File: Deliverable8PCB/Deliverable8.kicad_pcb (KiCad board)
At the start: 2 copper layers, 55 parts, among them J2 PiHeaderM, Q1 NMOS, Q2 PMOS, U1 MCP4131-xxxx-P, U10 MCP4131-xxxx-P, U11 MCP4131-xxxx-P, U12 LM741, U2 LM741, U3 LM741, U4 LM339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

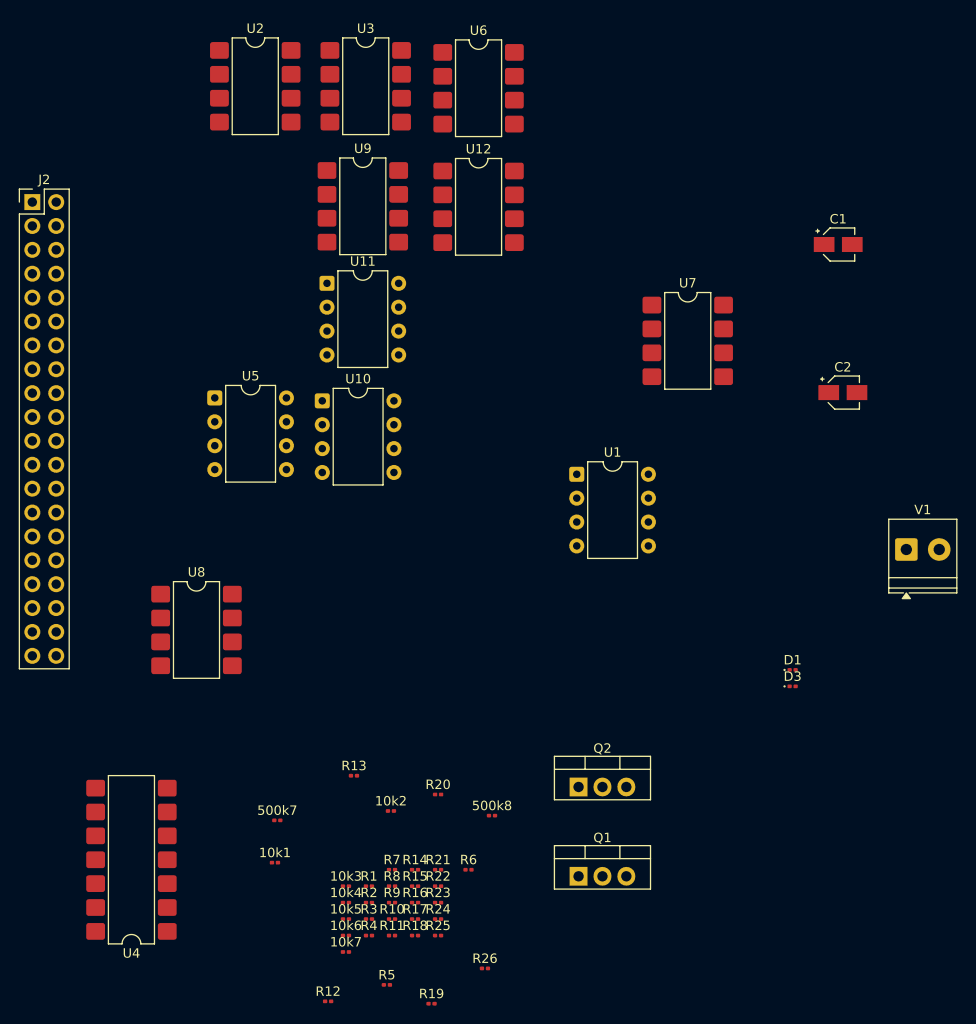
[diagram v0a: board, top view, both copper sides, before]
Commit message: update i2c_lcd
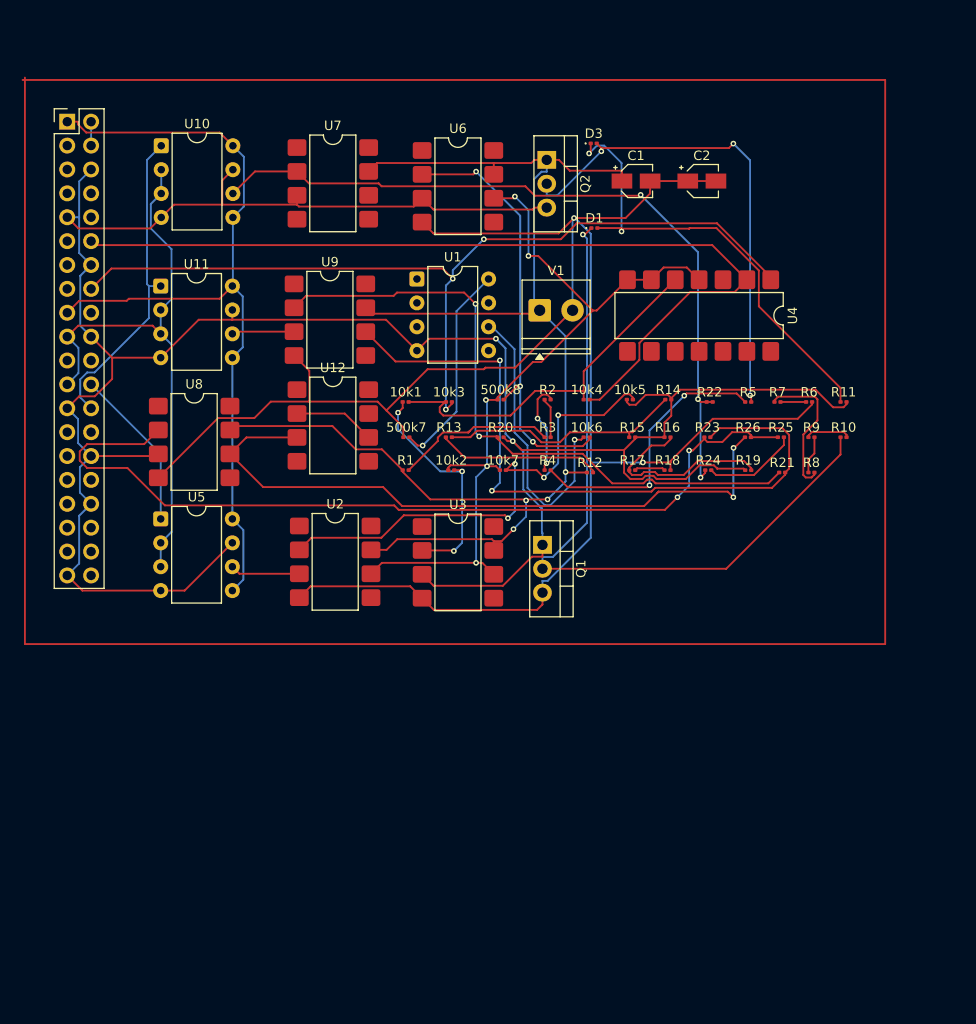
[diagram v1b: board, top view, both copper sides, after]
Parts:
- moved U4 83.6 mm to (109.7, 50.8), turned to -90 degrees
- moved R11 74.3 mm to (125.1, 60.0)
- moved R5 72.9 mm to (114.9, 60.0)
- moved R10 70.2 mm to (125.1, 63.8)
- moved Q2 66.8 mm to (93.5, 34.2), turned to -90 degrees
- moved R9 66.6 mm to (121.7, 63.8)
- moved R19 66.0 mm to (114.9, 67.2)
- moved R7 64.5 mm to (118.0, 60.0)
- moved R25 64.3 mm to (118.4, 63.8)
- moved R26 63.0 mm to (114.9, 63.8)
- moved 10k5 63.0 mm to (102.3, 59.8)
- moved R12 62.8 mm to (98.1, 67.5)
- moved R8 62.7 mm to (121.7, 67.5)
- moved R6 61.5 mm to (121.4, 60.0)
- moved D3 61.5 mm to (98.5, 32.5)
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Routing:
- net GND: track 0.00 -> 290.6 mm, vias 0 -> 2
- net -12V: track 0.00 -> 205.6 mm, vias 0 -> 2
- net +12V: track 0.00 -> 148.8 mm, vias 0 -> 4
- net /GPIO23*: track 0.00 -> 94.6 mm, vias 0 -> 3
- net /GPIO18*: track 0.00 -> 94.5 mm
- net Net-(U8--): track 0.00 -> 93.1 mm, vias 0 -> 2
- net /3V3GPIO*: track 0.00 -> 87.8 mm
- net Net-(U4A--): track 0.00 -> 86.7 mm, vias 0 -> 5
- net Net-(U10-P0W): track 0.00 -> 80.8 mm, vias 0 -> 3
- net Net-(D1-K): track 0.00 -> 78.1 mm, vias 0 -> 1
- net Net-(R21-Pad2): track 0.00 -> 75.3 mm, vias 0 -> 2
- net Net-(U12-+): track 0.00 -> 71.8 mm, vias 0 -> 2
- net Net-(U9--): track 0.00 -> 69.6 mm, vias 0 -> 2
- net /GPIO10*: track 0.00 -> 61.9 mm
- net Net-(D3-A): track 0.00 -> 52.6 mm, vias 0 -> 3
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
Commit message: added voltmeter
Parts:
- added C3: 470uF, Capacitor_SMD:CP_Elec_3x5.3, F.Cu at (102.5, 82.8)
- added R27: 100k, Resistor_SMD:R_0201_0603Metric, F.Cu at (109.8, 71.5)
- added R28: 10k, Resistor_SMD:R_0201_0603Metric, F.Cu at (110.1, 75.5)
- added R29: 70k, Resistor_SMD:R_0201_0603Metric, F.Cu at (104.3, 75.5)
- added U13: MCP4131-xxxx-P, Package_DIP:DIP-8_W7.62mm, F.Cu at (118.5, 33.5)
- added U14: TL081, Package_DIP:DIP-8_W7.62mm, F.Cu at (119.7, 74.7)
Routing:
- net /GPIO13*: track 0.00 -> 141.2 mm, vias 0 -> 1
- net /GPIO7*: track 33.9 -> 113.7 mm, vias 0 -> 2
- net /GPIO10*: track 61.9 -> 133.7 mm
- net GND: track 290.6 -> 359.8 mm, vias 2 -> 3
- net /3V3GPIO*: track 87.8 -> 156.4 mm
- net Net-(U13-P0W): track 0.00 -> 64.2 mm, vias 0 -> 1
- net +12V: track 148.8 -> 191.5 mm, vias 4 -> 5
- net Net-(R29-Pad2): track 0.00 -> 29.7 mm, vias 0 -> 2
- net -12V: track 205.6 -> 232.8 mm
- net Net-(U14--): track 0.00 -> 23.4 mm, vias 0 -> 1
- net Net-(C3-Pad1): track 0.00 -> 21.9 mm, vias 0 -> 2
- net Net-(U4A--): track 86.7 -> 86.2 mm
